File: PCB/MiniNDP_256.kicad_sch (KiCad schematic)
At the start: 18 parts, among them J1 Conn_02x20_Odd_Even, U1 74161, U2 74161, U3 74161, U4 74138, U5 74374, U6 AS6C2008A, U7 741G32

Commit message: minor sch alignment
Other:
- note added: "Each ~{BLOCK} pulse resets A0-A9 to 0, and sets A10-A17 from AD0-AD7 from the bus. (0-255) Each ~{BYTE} pulse increments A0-A9 by 1. (0-1023)"
- note removed: "Each ~{BLOCK} pulse resets A0-A9 to 0, and sets A10-A17 from BUS AD0-AD7. (0-255) Each ~{BYTE} pulse increments A0-A9 by 1. (0-1023)"
- moved on the sheet: U4
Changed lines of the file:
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@@
   (junction (at 134.62 179.07) (diameter 0) (color 0 0 0 0)
   )
-  (no_connect (at 72.39 57.15))
+  (no_connect (at 76.2 57.15))
   (no_connect (at 67.31 133.35))
   (no_connect (at 190.5 74.93))
   (no_connect (at 67.31 118.11))
-  (no_connect (at 72.39 62.23))
+  (no_connect (at 76.2 62.23))
   (no_connect (at 54.61 143.51))
   (no_connect (at 67.31 125.73))
-  (no_connect (at 72.39 69.85))
+  (no_connect (at 76.2 69.85))
   (no_connect (at 67.31 143.51))
   (no_connect (at 190.5 77.47))
@@
   (no_connect (at 190.5 82.55))
   (no_connect (at 54.61 115.57))
-  (no_connect (at 72.39 67.31))
+  (no_connect (at 76.2 67.31))
   (no_connect (at 54.61 118.11))
   (no_connect (at 54.61 135.89))
-  (no_connect (at 72.39 64.77))
+  (no_connect (at 76.2 64.77))
   (no_connect (at 67.31 113.03))
   (no_connect (at 54.61 128.27))
@@
   (no_connect (at 87.63 166.37))
   (no_connect (at 54.61 113.03))
-  (no_connect (at 72.39 52.07))
+  (no_connect (at 76.2 52.07))
   (bus_entry (at 194.31 72.39) (size 2.54 -2.54)
     (stroke (width 0) (type default))
@@
     (stroke (width 0) (type default))
   )
-  (wire (pts (xy 40.64 67.31) (xy 46.99 67.31))
+  (wire (pts (xy 40.64 67.31) (xy 50.8 67.31))
     (stroke (width 0) (type default))
   )
@@
     (stroke (width 0) (type default))
   )
-  (wire (pts (xy 72.39 59.69) (xy 95.25 59.69))
+  (wire (pts (xy 76.2 59.69) (xy 95.25 59.69))
     (stroke (width 0) (type default))
   )
@@
     (stroke (width 0) (type default))
   )
-  (wire (pts (xy 72.39 54.61) (xy 101.6 54.61))
+  (wire (pts (xy 76.2 54.61) (xy 101.6 54.61))
     (stroke (width 0) (type default))
   )
@@
     (stroke (width 0) (type default))
   )
-  (wire (pts (xy 40.64 64.77) (xy 46.99 64.77))
+  (wire (pts (xy 40.64 64.77) (xy 50.8 64.77))
     (stroke (width 0) (type default))
   )
@@
     (stroke (width 0) (type default))
   )
-  (wire (pts (xy 40.64 52.07) (xy 46.99 52.07))
+  (wire (pts (xy 40.64 52.07) (xy 50.8 52.07))
     (stroke (width 0) (type default))
   )
@@
     (stroke (width 0) (type default))
   )
-  (wire (pts (xy 40.64 54.61) (xy 46.99 54.61))
+  (wire (pts (xy 40.64 54.61) (xy 50.8 54.61))
     (stroke (width 0) (type default))
   )
@@
     (effects (font (size 1.27 1.27)) (justify left bottom))
   )
-  (text "Each ~{BLOCK} pulse resets A0-A9 to 0,\nand sets A10-A17 from BUS AD0-AD7. (0-255)\n\nEach ~{BYTE} pulse increments A0-A9 by 1. (0-1023)\n"
-    (at 34.29 35.56 0)
+  (text "Each ~{BLOCK} pulse resets A0-A9 to 0, and\nsets A10-A17 from AD0-AD7 from the bus. (0-255)\n\nEach ~{BYTE} pulse increments A0-A9 by 1. (0-1023)\n"
+    (at 36.83 35.56 0)
     (effects (font (size 1.27 1.27)) (justify left bottom))
   )
@@
     (effects (font (size 1.27 1.27)) (justify right bottom))
   )
-  (label "Y0" (at 46.99 67.31 180) (fields_autoplaced)
+  (label "Y0" (at 50.8 67.31 180) (fields_autoplaced)
     (effects (font (size 1.27 1.27)) (justify right bottom))
   )
@@
     (effects (font (size 1.27 1.27)) (justify left bottom))
   )
-  (label "~{BLOCK}" (at 72.39 54.61 0) (fields_autoplaced)
+  (label "~{BLOCK}" (at 76.2 54.61 0) (fields_autoplaced)
     (effects (font (size 1.27 1.27)) (justify left bottom))
   )
@@
     (effects (font (size 1.27 1.27)) (justify right bottom))
   )
-  (label "~{A}" (at 46.99 64.77 180) (fields_autoplaced)
+  (label "~{A}" (at 50.8 64.77 180) (fields_autoplaced)
     (effects (font (size 1.27 1.27)) (justify right bottom))
   )
@@
     (effects (font (size 1.27 1.27)) (justify left bottom))
   )
-  (label "BUS_A9" (at 46.99 54.61 180) (fields_autoplaced)
+  (label "BUS_A9" (at 50.8 54.61 180) (fields_autoplaced)
     (effects (font (size 1.27 1.27)) (justify right bottom))
   )
@@
     (effects (font (size 1.27 1.27)) (justify right bottom))
   )
-  (label "BUS_A8" (at 46.99 52.07 180) (fields_autoplaced)
+  (label "BUS_A8" (at 50.8 52.07 180) (fields_autoplaced)
     (effects (font (size 1.27 1.27)) (justify right bottom))
   )
@@
     (effects (font (size 1.27 1.27)) (justify left bottom))
   )
-  (label "~{BYTE}" (at 72.39 59.69 0) (fields_autoplaced)
+  (label "~{BYTE}" (at 76.2 59.69 0) (fields_autoplaced)
     (effects (font (size 1.27 1.27)) (justify left bottom))
   )
@@
     )
   )
-  (symbol (lib_id "power:GND") (at 59.69 77.47 0) (unit 1)
-    (in_bom yes) (on_board yes) (dnp no)
-    (property "Reference" "#PWR022" (at 59.69 83.82 0)
-      (effects (font (size 1.27 1.27)) hide)
-    )
-    (property "Value" "GND" (at 55.88 80.01 0)
-      (effects (font (size 1.27 1.27)))
-    )
-    (property "Footprint" "" (at 59.69 77.47 0)
-      (effects (font (size 1.27 1.27)) hide)
-    )
-    (property "Datasheet" "" (at 59.69 77.47 0)
+  (symbol (lib_id "power:GND") (at 63.5 77.47 0) (unit 1)
+    (in_bom yes) (on_board yes) (dnp no)
+    (property "Reference" "#PWR022" (at 63.5 83.82 0)
+      (effects (font (size 1.27 1.27)) hide)
+    )
+    (property "Value" "GND" (at 59.69 80.01 0)
+      (effects (font (size 1.27 1.27)))
+    )
+    (property "Footprint" "" (at 63.5 77.47 0)
+      (effects (font (size 1.27 1.27)) hide)
+    )
+    (property "Datasheet" "" (at 63.5 77.47 0)
       (effects (font (size 1.27 1.27)) hide)
     )
@@
     )
   )
-  (symbol (lib_id "power:GND") (at 46.99 57.15 270) (unit 1)
-    (in_bom yes) (on_board yes) (dnp no)
-    (property "Reference" "#PWR037" (at 40.64 57.15 0)
-      (effects (font (size 1.27 1.27)) hide)
-    )
-    (property "Value" "GND" (at 46.99 59.69 90)
+  (symbol (lib_id "power:GND") (at 50.8 57.15 270) (unit 1)
+    (in_bom yes) (on_board yes) (dnp no)
+    (property "Reference" "#PWR037" (at 44.45 57.15 0)
+      (effects (font (size 1.27 1.27)) hide)
+    )
+    (property "Value" "GND" (at 50.8 59.69 90)
       (effects (font (size 1.27 1.27)) (justify right))
     )
-    (property "Footprint" "" (at 46.99 57.15 0)
-      (effects (font (size 1.27 1.27)) hide)
-    )
-    (property "Datasheet" "" (at 46.99 57.15 0)
+    (property "Footprint" "" (at 50.8 57.15 0)
+      (effects (font (size 1.27 1.27)) hide)
+    )
+    (property "Datasheet" "" (at 50.8 57.15 0)
       (effects (font (size 1.27 1.27)) hide)
     )
@@
     )
   )
-  (symbol (lib_id "000_LOCAL:74138") (at 59.69 59.69 0) (unit 1)
+  (symbol (lib_id "000_LOCAL:74138") (at 63.5 59.69 0) (unit 1)
     (in_bom yes) (on_board yes) (dnp no) (fields_autoplaced)
-    (property "Reference" "U4" (at 61.8841 44.45 0)
+    (property "Reference" "U4" (at 65.6941 44.45 0)
       (effects (font (size 1.27 1.27)) (justify left))
     )
-    (property "Value" "74138" (at 61.8841 46.99 0)
+    (property "Value" "74138" (at 65.6941 46.99 0)
       (effects (font (size 1.27 1.27)) (justify left))
     )
-    (property "Footprint" "000_LOCAL:TSSOP-16" (at 59.69 59.69 0)
-      (effects (font (size 1.27 1.27)) hide)
-    )
-    (property "Datasheet" "datasheets/74HC138.pdf" (at 59.69 59.69 0)
+    (property "Footprint" "000_LOCAL:TSSOP-16" (at 63.5 59.69 0)
+      (effects (font (size 1.27 1.27)) hide)
+    )
+    (property "Datasheet" "datasheets/74HC138.pdf" (at 63.5 59.69 0)
       (effects (font (size 1.27 1.27)) hide)
     )
@@
     )
   )
-  (symbol (lib_id "power:GND") (at 46.99 69.85 270) (unit 1)
+  (symbol (lib_id "power:GND") (at 50.8 69.85 270) (unit 1)
     (in_bom yes) (on_board yes) (dnp no) (fields_autoplaced)
-    (property "Reference" "#PWR038" (at 40.64 69.85 0)
-      (effects (font (size 1.27 1.27)) hide)
-    )
-    (property "Value" "GND" (at 43.18 69.85 90)
+    (property "Reference" "#PWR038" (at 44.45 69.85 0)
+      (effects (font (size 1.27 1.27)) hide)
+    )
+    (property "Value" "GND" (at 46.99 69.85 90)
       (effects (font (size 1.27 1.27)) (justify right))
     )
-    (property "Footprint" "" (at 46.99 69.85 0)
-      (effects (font (size 1.27 1.27)) hide)
-    )
-    (property "Datasheet" "" (at 46.99 69.85 0)
+    (property "Footprint" "" (at 50.8 69.85 0)
+      (effects (font (size 1.27 1.27)) hide)
+    )
+    (property "Datasheet" "" (at 50.8 69.85 0)
       (effects (font (size 1.27 1.27)) hide)
     )
@@
     )
   )
-  (symbol (lib_id "power:VBUS") (at 59.69 44.45 0) (unit 1)
-    (in_bom yes) (on_board yes) (dnp no)
-    (property "Reference" "#PWR033" (at 59.69 48.26 0)
-      (effects (font (size 1.27 1.27)) hide)
-    )
-    (property "Value" "VBUS" (at 55.88 41.91 0)
-      (effects (font (size 1.27 1.27)))
-    )
-    (property "Footprint" "" (at 59.69 44.45 0)
-      (effects (font (size 1.27 1.27)) hide)
-    )
-    (property "Datasheet" "" (at 59.69 44.45 0)
-      (effects (font (size 1.27 1.27)) hide)
-    )
+  (symbol (lib_id "power:VBUS") (at 63.5 44.45 0) (unit 1)
+    (in_bom yes) (on_board yes) (dnp no)
+    (property "Reference" "#PWR033" (at 63.5 48.26 0)
+      (effects (font (size 1.27 1.27)) hide)
+    )
+    (property "Value" "VBUS" (at 59.69 41.91 0)
+      (effects (font (size 1.27 1.27)))
+    )
+    (property "Footprint" "" (at 63.5 44.45 0)
+      (effects (font (size 1.27 1.27)) hide)
+    )
+    (property "Datasheet" "" (at 63.5 44.45 0)
+      (effects (font (size 1.27 1.27)) hide)
+    )

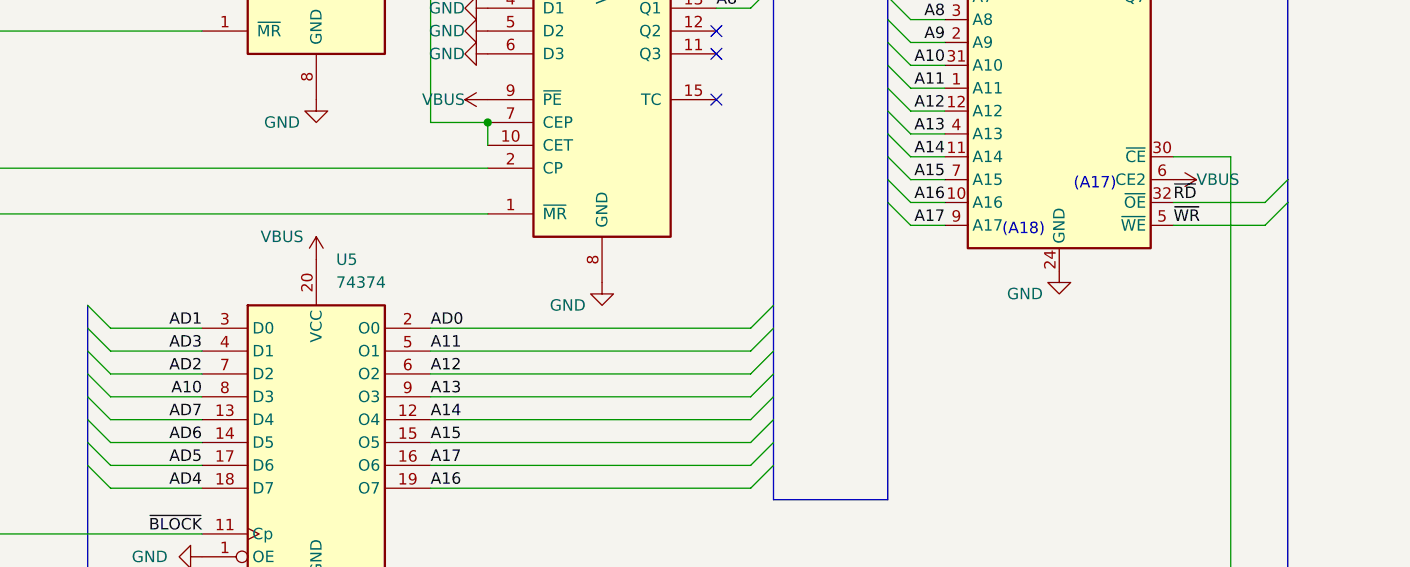
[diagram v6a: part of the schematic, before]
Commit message: minindp fix swapped AD0 vs A10 on U5, improve routing
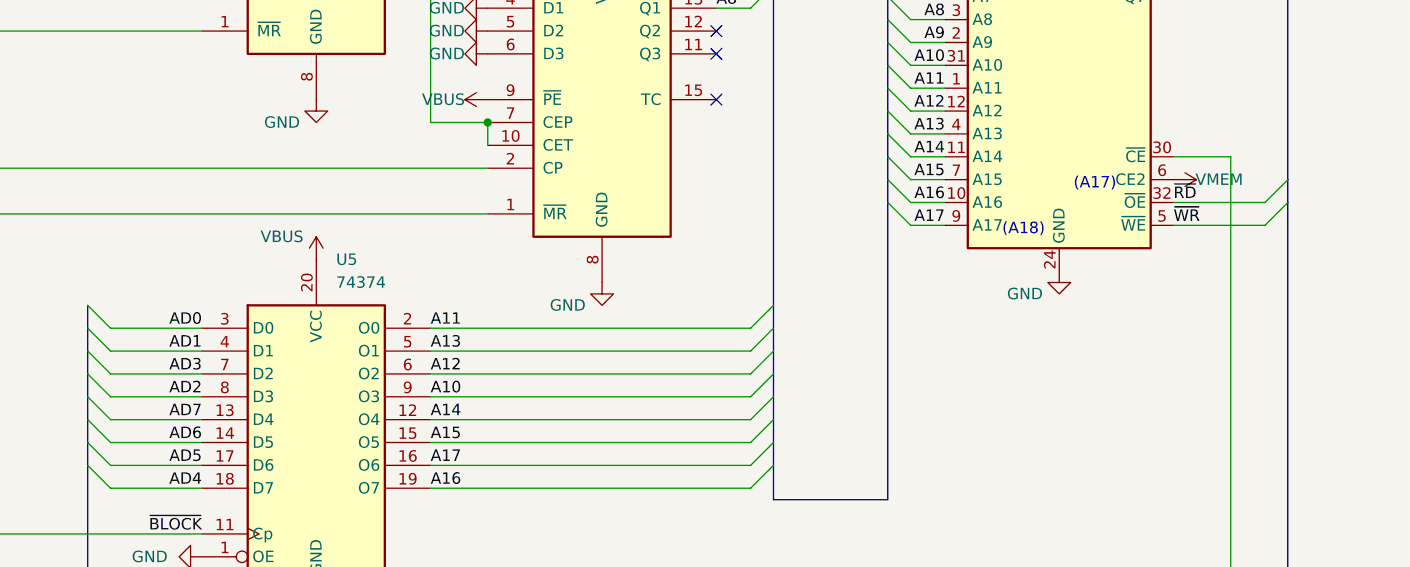
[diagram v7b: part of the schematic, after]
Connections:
- net A10: now also U5.9 (O3); no longer U5.8 (D3)
- net A11: now also U5.2 (O0); no longer U5.5 (O1)
- net A13: now also U5.5 (O1); no longer U5.9 (O3)
- net AD0: now also U5.3 (D0); no longer U5.2 (O0)
- net AD1: now also U5.4 (D1); no longer U5.3 (D0)
- net AD2: now also U5.8 (D3); no longer U5.7 (D2)
- net AD3: now also U5.7 (D2); no longer U5.4 (D1)
- net VBUS: no longer U6.6 (CE2)
- net VMEM: now also U6.6 (CE2)
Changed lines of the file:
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@@
   (title_block
     (title "MiniNDP 256")
-    (date "2023-08-29")
-    (rev "002")
+    (date "2023-08-30")
+    (rev "003")
     (company "Brian K. White - b.kenyon.w@gmail.com")
     (comment 1 "Work-alike of NODE DATAPAC 256k")
@@
     (effects (font (size 1.27 1.27)) (justify right bottom))
   )
-  (label "A11" (at 158.75 110.49 0) (fields_autoplaced)
+  (label "A11" (at 158.75 107.95 0) (fields_autoplaced)
     (effects (font (size 1.27 1.27)) (justify left bottom))
   )
@@
     (effects (font (size 1.27 1.27)) (justify left bottom))
   )
-  (label "A10" (at 133.35 115.57 180) (fields_autoplaced)
-    (effects (font (size 1.27 1.27)) (justify right bottom))
+  (label "A10" (at 158.75 115.57 0) (fields_autoplaced)
+    (effects (font (size 1.27 1.27)) (justify left bottom))
   )
   (label "RAM_RST" (at 54.61 140.97 180) (fields_autoplaced)
@@
     (effects (font (size 1.27 1.27)) (justify right bottom))
   )
-  (label "AD0" (at 158.75 107.95 0) (fields_autoplaced)
-    (effects (font (size 1.27 1.27)) (justify left bottom))
+  (label "AD0" (at 133.35 107.95 180) (fields_autoplaced)
+    (effects (font (size 1.27 1.27)) (justify right bottom))
   )
   (label "A3" (at 215.9 60.96 180) (fields_autoplaced)
@@
     (effects (font (size 1.27 1.27)) (justify left bottom))
   )
-  (label "AD2" (at 133.35 113.03 180) (fields_autoplaced)
+  (label "AD2" (at 133.35 115.57 180) (fields_autoplaced)
     (effects (font (size 1.27 1.27)) (justify right bottom))
   )
@@
     (effects (font (size 1.27 1.27)) (justify left bottom))
   )
-  (label "A13" (at 158.75 115.57 0) (fields_autoplaced)
+  (label "A13" (at 158.75 110.49 0) (fields_autoplaced)
     (effects (font (size 1.27 1.27)) (justify left bottom))
   )
@@
     (effects (font (size 1.27 1.27)) (justify right bottom))
   )
-  (label "AD1" (at 133.35 107.95 180) (fields_autoplaced)
+  (label "AD1" (at 133.35 110.49 180) (fields_autoplaced)
     (effects (font (size 1.27 1.27)) (justify right bottom))
   )
@@
     (effects (font (size 1.27 1.27)) (justify right bottom))
   )
-  (label "AD3" (at 133.35 110.49 180) (fields_autoplaced)
+  (label "AD3" (at 133.35 113.03 180) (fields_autoplaced)
     (effects (font (size 1.27 1.27)) (justify right bottom))
   )
@@
     )
   )
-  (symbol (lib_id "power:VBUS") (at 241.3 91.44 270) (unit 1)
-    (in_bom yes) (on_board yes) (dnp no)
-    (property "Reference" "#PWR024" (at 237.49 91.44 0)
-      (effects (font (size 1.27 1.27)) hide)
-    )
-    (property "Value" "VBUS" (at 243.84 91.44 90)
-      (effects (font (size 1.27 1.27)) (justify left))
-    )
-    (property "Footprint" "" (at 241.3 91.44 0)
-      (effects (font (size 1.27 1.27)) hide)
-    )
-    (property "Datasheet" "" (at 241.3 91.44 0)
-      (effects (font (size 1.27 1.27)) hide)
-    )
-    (pin "1")
-    (instances
-      (project "MiniNDP_256"
-        (path "/f15c2929-5cf4-4b4e-965d-148e1bec8a42"
-          (reference "#PWR024") (unit 1)
-        )
-      )
-    )
-  )
   (symbol (lib_id "000_LOCAL:74374") (at 146.05 120.65 0) (unit 1)
     (in_bom yes) (on_board yes) (dnp no) (fields_autoplaced)
@@
     )
   )
+  (symbol (lib_id "000_LOCAL:VMEM") (at 241.3 91.44 270) (unit 1)
+    (in_bom yes) (on_board yes) (dnp no)
+    (property "Reference" "#PWR024" (at 237.49 91.44 0)
+      (effects (font (size 1.27 1.27)) hide)
+    )
+    (property "Value" "VMEM" (at 246.38 91.44 90)
+      (effects (font (size 1.27 1.27)))
+    )
+    (property "Footprint" "" (at 241.3 91.44 0)
+      (effects (font (size 1.27 1.27)) hide)
+    )
+    (property "Datasheet" "" (at 241.3 91.44 0)
+      (effects (font (size 1.27 1.27)) hide)
+    )
+    (pin "1")
+    (instances
+      (project "MiniNDP_256"
+        (path "/f15c2929-5cf4-4b4e-965d-148e1bec8a42"
+          (reference "#PWR024") (unit 1)
+        )
+      )
+      (project "TANDY_600_RAM_DUAL"
+        (path "/fe5b516f-55dc-44bb-a7ae-e479a38db771"
+          (reference "#PWR0115") (unit 1)
+        )
+      )
+    )
+  )
   (symbol (lib_name "BAV70_1") (lib_id "000_LOCAL:BAV70") (at 87.63 158.75 270) (mirror x) (unit 1)
     (in_bom yes) (on_board yes) (dnp no)
@@
       (effects (font (size 1.27 1.27)) hide)
     )
-    (property "Datasheet" "~" (at 62.23 118.11 0)
-      (effects (font (size 1.27 1.27)) hide)
-    )
+    (property "Datasheet" "datasheets/2x20_male_boxed.pdf" (at 62.23 118.11 0)
+      (effects (font (size 1.27 1.27)) hide)
+    )

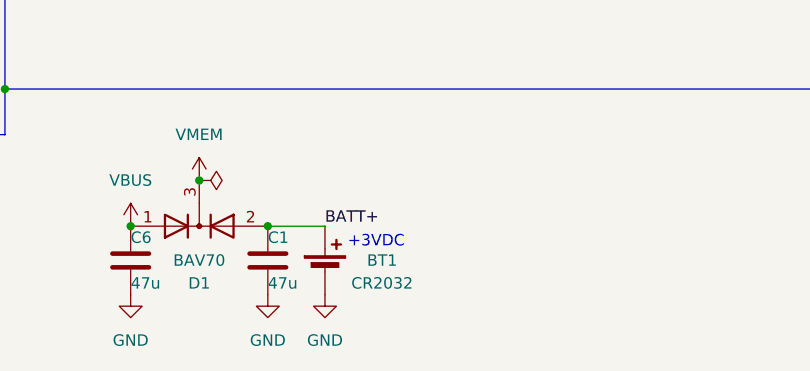
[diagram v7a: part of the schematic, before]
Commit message: minindp battery holder part number
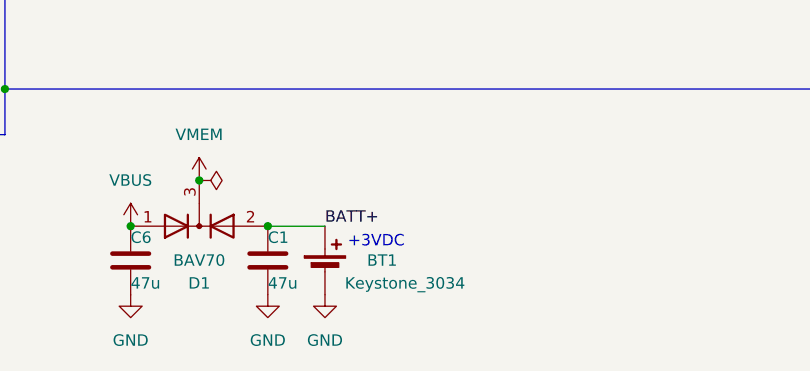
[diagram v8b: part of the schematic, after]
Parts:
- BT1: value CR2032 -> Keystone_3034
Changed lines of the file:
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@@
       (effects (font (size 1.27 1.27)))
     )
-    (property "Value" "CR2032" (at 162.56 185.42 0)
+    (property "Value" "Keystone_3034" (at 165.1 185.42 0)
       (effects (font (size 1.27 1.27)))
     )
